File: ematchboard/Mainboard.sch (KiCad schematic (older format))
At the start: 45 parts, among them J10 Conn_01x02_Male, J9 Conn_01x02_Male, Q1 MMDT2222A, U2 SN65HVD230, U3 ESP32-WROOM-32D

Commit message: Added arming LED
Arming LED is to turn ON when circuit is primed - after 5s of charging capacitor / boot
A more precise way to do this would probably be to hook up another MOSFET to regulate input voltage  (so you can control capacitor charging from the ESP)
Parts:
- added D?: LED, symbol Device:LED
- added R?: 470, symbol Device:R_Small
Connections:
- net GND: now also D?.1 (K)
- net ARM_LED: now reaches U3.10 (IO25)
- net ARM_LED: now also R?.1
- new net: D?.2 (A), R?.2
- no-connect marks 24 -> 29
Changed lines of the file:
@@
 $EndComp
-Wire Wire Line
-	2200 1000 2200 1750
 Wire Wire Line
 	1300 1000 1450 1000
@@
 Text Notes 9150 600  0    50   ~ 0
 This can be expanded to as many pins are available
+Wire Wire Line
+	2200 1000 2200 1750
+NoConn ~ 7000 5050
+NoConn ~ 7000 5150
+NoConn ~ 7000 5250
+NoConn ~ 7000 5950
+NoConn ~ 7000 6050
+Text Label 7350 5850 2    50   ~ 0
+ARM_LED
+Wire Wire Line
+	7350 5850 7000 5850
+$Comp
+L Device:LED D?
+U 1 1 61B402D1
+P 4400 1550
+F 0 "D?" V 4439 1432 50  0000 R CNN
+F 1 "LED" V 4348 1432 50  0000 R CNN
+F 2 "" H 4400 1550 50  0001 C CNN
+F 3 "~" H 4400 1550 50  0001 C CNN
+	1    4400 1550
+	0    -1   -1   0
+$EndComp
+$Comp
+L Device:R_Small R?
+U 1 1 61B402D7
+P 4400 1300
+F 0 "R?" H 4459 1346 50  0000 L CNN
+F 1 "470" H 4459 1255 50  0000 L CNN
+F 2 "" H 4400 1300 50  0001 C CNN
+F 3 "~" H 4400 1300 50  0001 C CNN
+	1    4400 1300
+	1    0    0    -1
+$EndComp
+Text Label 4100 1000 0    50   ~ 0
+ARM_LED
+Wire Wire Line
+	4400 1000 4400 1200
+$Comp
+L power:GND #PWR?
+U 1 1 61B402E0
+P 4400 1800
+F 0 "#PWR?" H 4400 1550 50  0001 C CNN
+F 1 "GND" H 4405 1627 50  0000 C CNN
+F 2 "" H 4400 1800 50  0001 C CNN
+F 3 "" H 4400 1800 50  0001 C CNN
+	1    4400 1800
+	1    0    0    -1
+$EndComp
+Wire Wire Line
+	4400 1800 4400 1700
+Wire Wire Line
+	4100 1000 4400 1000
 $EndSCHEMATC

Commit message: Added arming LED 2
Github Desktop threw me a weird error, so here's a second commit
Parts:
- ANT?: symbol AMCA31-2R450G-S1F-T3:AMCA31-2R450G-S1F-T3 -> Mainboard-rescue:AMCA31-2R450G-S1F-T3-AMCA31-2R450G-S1F-T3
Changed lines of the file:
@@
 NoConn ~ 7000 6450
 $Comp
-L AMCA31-2R450G-S1F-T3:AMCA31-2R450G-S1F-T3 ANT?
+L Mainboard-rescue:AMCA31-2R450G-S1F-T3-AMCA31-2R450G-S1F-T3 ANT?
 U 1 1 619C5032
 P 7450 1050

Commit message: Schematic comments + minor fixes
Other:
- note added: "It might also be desirable to control charging from the ESP - \nthen a transistor could be used between 3.3V and the input voltage \nfor the ignitor circuits - rather than charging starting automatically \nonce the buck-boost starts operating\n"
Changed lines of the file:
@@
 Text Label 7350 4650 2    50   ~ 0
 MTCH_0
-Text Label 10250 800  0    50   ~ 0
+Text Label 9550 6000 0    50   ~ 0
 MTCH_0
-Text Label 10250 900  0    50   ~ 0
+Text Label 9550 6100 0    50   ~ 0
 MTCH_1
-Text Label 10250 1000 0    50   ~ 0
+Text Label 9550 6200 0    50   ~ 0
 MTCH_2
-Text Label 10250 1100 0    50   ~ 0
+Text Label 9550 6300 0    50   ~ 0
 MTCH_3
 Wire Wire Line
-	10250 800  10600 800
+	9550 6000 9900 6000
 Wire Wire Line
-	10600 900  10250 900
+	9900 6100 9550 6100
 Wire Wire Line
-	10250 1000 10600 1000
+	9550 6200 9900 6200
 Wire Wire Line
-	10600 1100 10250 1100
+	9900 6300 9550 6300
 Text Label 7350 4750 2    50   ~ 0
 MTCH_1
@@
 SCLK
 $Sheet
-S 10600 750  550  450
+S 9900 5950 550  450
 U 61C80F8F
 F0 "ematch" 50
 F1 "ematch.sch" 50
-F2 "IGN_0" I L 10600 800 50
-F3 "IGN_1" I L 10600 900 50
-F4 "IGN_2" I L 10600 1000 50
-F5 "IGN_3" I L 10600 1100 50
+F2 "IGN_0" I L 9900 6000 50
+F3 "IGN_1" I L 9900 6100 50
+F4 "IGN_2" I L 9900 6200 50
+F5 "IGN_3" I L 9900 6300 50
 $EndSheet
-Text Notes 9150 600  0    50   ~ 0
+Text Notes 8450 5800 0    50   ~ 0
 This can be expanded to as many pins are available
 Wire Wire Line
@@
 Wire Wire Line
 	4100 1000 4400 1000
+Text Notes 8450 5600 0    50   ~ 0
+It might also be desirable to control charging from the ESP - \nthen a transistor could be used between 3.3V and the input voltage \nfor the ignitor circuits - rather than charging starting automatically \nonce the buck-boost starts operating\n
 $EndSCHEMATC

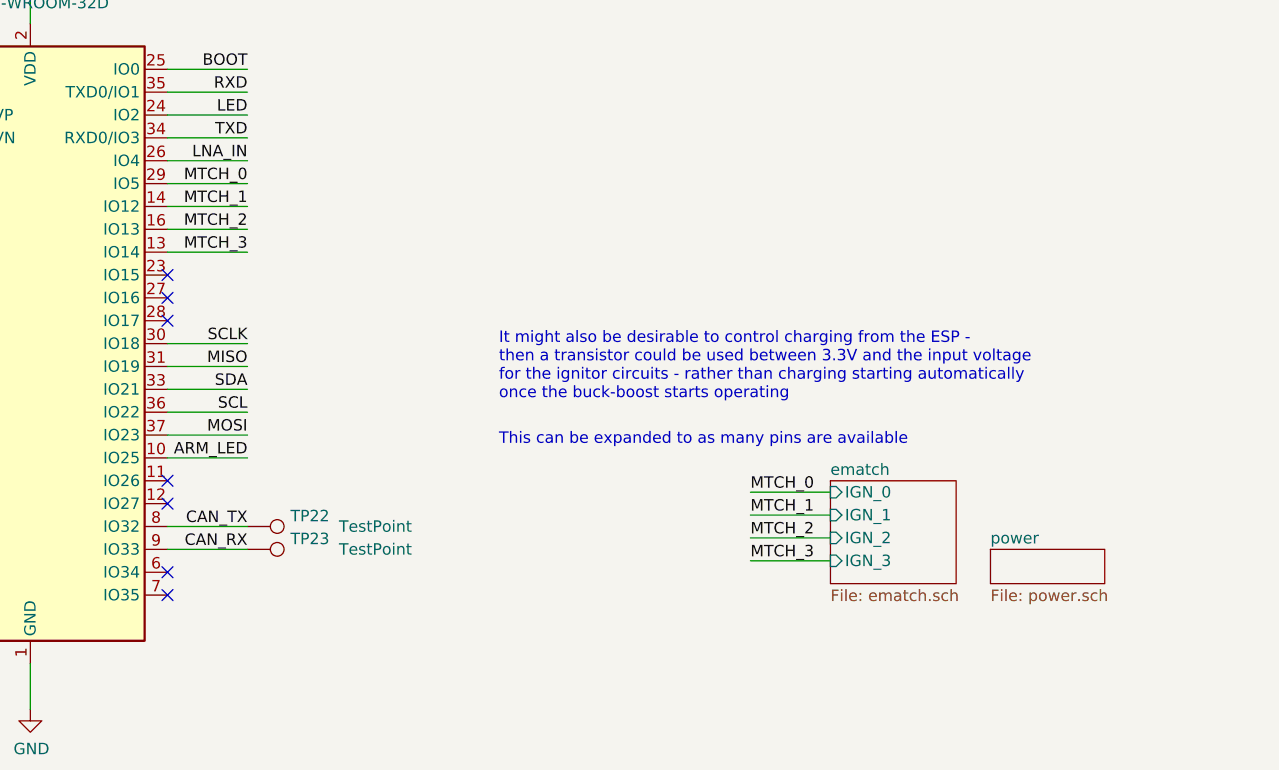
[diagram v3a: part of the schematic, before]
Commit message: Updated number of ematches
Increased e match count from 4->6 as requested (2 spares)
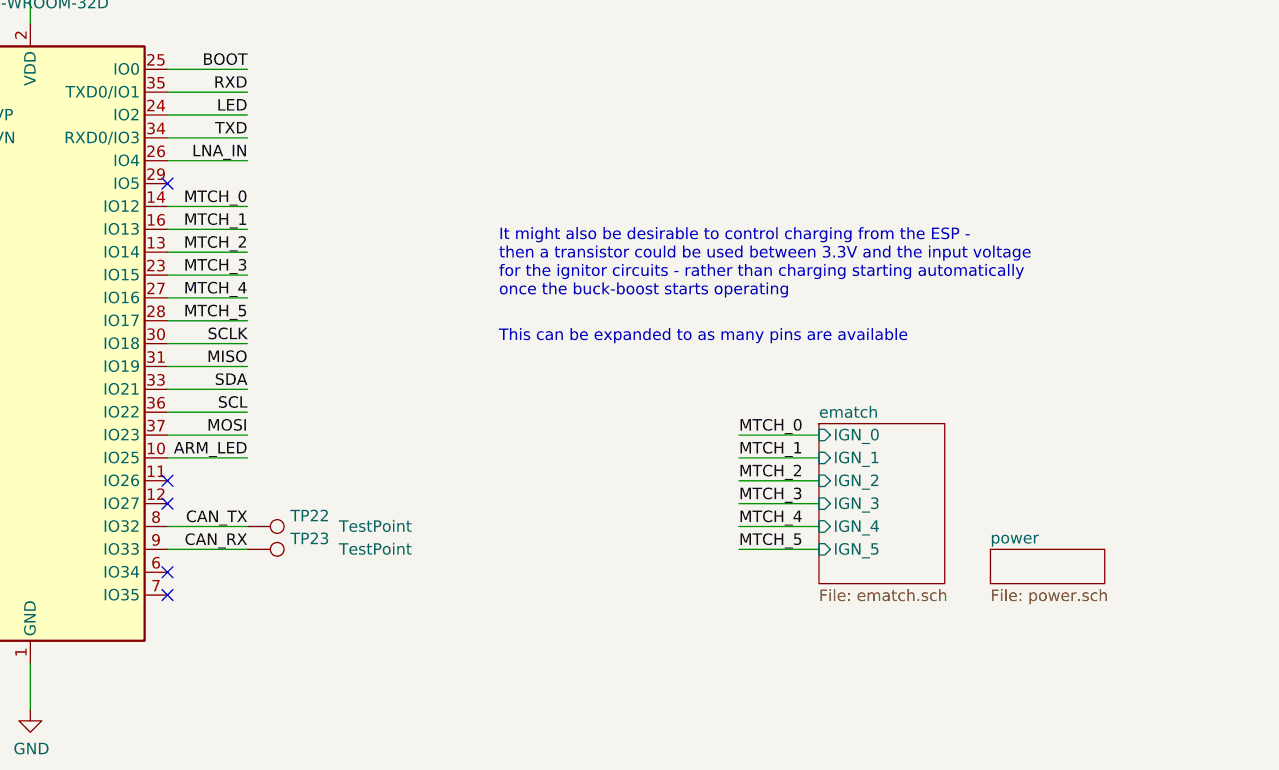
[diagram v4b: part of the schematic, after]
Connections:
- net MTCH_0: now also U3.14 (IO12); no longer U3.29 (IO5)
- net MTCH_1: now also U3.16 (IO13); no longer U3.14 (IO12)
- net MTCH_2: now also U3.13 (IO14); no longer U3.16 (IO13)
- net MTCH_3: now also U3.23 (IO15); no longer U3.13 (IO14)
- net MTCH_4: now reaches U3.27 (IO16)
- net MTCH_5: now reaches U3.28 (IO17)
- no-connect marks 29 -> 27
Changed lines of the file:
@@
 Wire Wire Line
 	7000 4150 7350 4150
-$Comp
-L RF_Module:ESP32-WROOM-32 U3
-U 1 1 5DA5F4C7
-P 6400 5350
-F 0 "U3" H 6400 6931 50  0000 C CNN
-F 1 "ESP32-WROOM-32D" H 6400 6840 50  0000 C CNN
-F 2 "RF_Module:ESP32-WROOM-32" H 6400 3850 50  0001 C CNN
-F 3 "https://www.espressif.com/sites/default/files/documentation/esp32-wroom-32d_esp32-wroom-32u_datasheet_en.pdf" H 6100 5400 50  0001 C CNN
-	1    6400 5350
-	1    0    0    -1
-$EndComp
 NoConn ~ 7000 6350
 NoConn ~ 7000 6450
@@
 Connection ~ 7450 1800
 Wire Wire Line
-	7350 4650 7000 4650
-Text Label 7350 4650 2    50   ~ 0
+	7350 4750 7000 4750
+Text Label 7350 4750 2    50   ~ 0
 MTCH_0
-Text Label 9550 6000 0    50   ~ 0
+Text Label 9500 5750 0    50   ~ 0
 MTCH_0
-Text Label 9550 6100 0    50   ~ 0
+Text Label 9500 5850 0    50   ~ 0
 MTCH_1
-Text Label 9550 6200 0    50   ~ 0
+Text Label 9500 5950 0    50   ~ 0
 MTCH_2
-Text Label 9550 6300 0    50   ~ 0
+Text Label 9500 6050 0    50   ~ 0
 MTCH_3
 Wire Wire Line
-	9550 6000 9900 6000
-Wire Wire Line
-	9900 6100 9550 6100
-Wire Wire Line
-	9550 6200 9900 6200
-Wire Wire Line
-	9900 6300 9550 6300
-Text Label 7350 4750 2    50   ~ 0
+	9500 5750 9850 5750
+Wire Wire Line
+	9850 5850 9500 5850
+Wire Wire Line
+	9500 5950 9850 5950
+Wire Wire Line
+	9850 6050 9500 6050
+Text Label 7350 4850 2    50   ~ 0
 MTCH_1
-Text Label 7350 4850 2    50   ~ 0
+Text Label 7350 4950 2    50   ~ 0
 MTCH_2
-Text Label 7350 4950 2    50   ~ 0
+Text Label 7350 5050 2    50   ~ 0
 MTCH_3
 Wire Wire Line
-	7350 4950 7000 4950
-Wire Wire Line
-	7000 4850 7350 4850
-Wire Wire Line
-	7350 4750 7000 4750
+	7350 5050 7000 5050
+Wire Wire Line
+	7000 4950 7350 4950
+Wire Wire Line
+	7350 4850 7000 4850
 Wire Wire Line
 	7000 5550 7350 5550
@@
 SCLK
 $Sheet
-S 9900 5950 550  450
+S 9850 5700 550  700
 U 61C80F8F
 F0 "ematch" 50
 F1 "ematch.sch" 50
-F2 "IGN_0" I L 9900 6000 50
-F3 "IGN_1" I L 9900 6100 50
-F4 "IGN_2" I L 9900 6200 50
-F5 "IGN_3" I L 9900 6300 50
+F2 "IGN_0" I L 9850 5750 50
+F3 "IGN_1" I L 9850 5850 50
+F4 "IGN_2" I L 9850 5950 50
+F5 "IGN_3" I L 9850 6050 50
+F6 "IGN_4" I L 9850 6150 50
+F7 "IGN_5" I L 9850 6250 50
 $EndSheet
-Text Notes 8450 5800 0    50   ~ 0
+Text Notes 8450 5350 0    50   ~ 0
 This can be expanded to as many pins are available
 Wire Wire Line
 	2200 1000 2200 1750
-NoConn ~ 7000 5050
-NoConn ~ 7000 5150
-NoConn ~ 7000 5250
 NoConn ~ 7000 5950
 NoConn ~ 7000 6050
@@
 Wire Wire Line
 	4100 1000 4400 1000
-Text Notes 8450 5600 0    50   ~ 0
+Text Notes 8450 5150 0    50   ~ 0
 It might also be desirable to control charging from the ESP - \nthen a transistor could be used between 3.3V and the input voltage \nfor the ignitor circuits - rather than charging starting automatically \nonce the buck-boost starts operating\n
+$Comp
+L RF_Module:ESP32-WROOM-32 U3
+U 1 1 5DA5F4C7
+P 6400 5350
+F 0 "U3" H 6400 6931 50  0000 C CNN
+F 1 "ESP32-WROOM-32D" H 6400 6840 50  0000 C CNN
+F 2 "RF_Module:ESP32-WROOM-32" H 6400 3850 50  0001 C CNN
+F 3 "https://www.espressif.com/sites/default/files/documentation/esp32-wroom-32d_esp32-wroom-32u_datasheet_en.pdf" H 6100 5400 50  0001 C CNN
+	1    6400 5350
+	1    0    0    -1
+$EndComp
+NoConn ~ 7000 4650
+Text Label 7350 5150 2    50   ~ 0
+MTCH_4
+Text Label 7350 5250 2    50   ~ 0
+MTCH_5
+Wire Wire Line
+	7350 5250 7000 5250
+Wire Wire Line
+	7000 5150 7350 5150
+Text Label 9500 6150 0    50   ~ 0
+MTCH_4
+Text Label 9500 6250 0    50   ~ 0
+MTCH_5
+Wire Wire Line
+	9500 6150 9850 6150
+Wire Wire Line
+	9850 6250 9500 6250
 $EndSCHEMATC
